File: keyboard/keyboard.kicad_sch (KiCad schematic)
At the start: 115 parts, among them J1 USB_C_Receptacle_USB2.0_14P, SW1 Keyswitch, SW10 Keyswitch, SW11 Keyswitch, SW12 Keyswitch, SW13 Keyswitch, SW14 Keyswitch, SW15 Keyswitch, SW16 Keyswitch, SW17 Keyswitch, SW18 Keyswitch, SW19 Keyswitch, SW2 Keyswitch, SW20 Keyswitch, SW21 Keyswitch, SW22 Keyswitch, SW23 Keyswitch, SW24 Keyswitch, SW25 Keyswitch, SW26 Keyswitch, SW27 Keyswitch, SW28 Keyswitch, SW29 Keyswitch, SW3 Keyswitch, SW30 Keyswitch, SW31 Keyswitch, SW32 Keyswitch, SW33 Keyswitch, SW34 Keyswitch, SW35 Keyswitch, SW36 Keyswitch, SW37 Keyswitch, SW38 Keyswitch, SW39 Keyswitch, SW4 Keyswitch, SW40 Keyswitch, SW41 Keyswitch, SW42 Keyswitch, SW43 Keyswitch, SW44 Keyswitch, SW45 Keyswitch, SW46 Keyswitch, SW47 Keyswitch, SW48 Keyswitch, SW5 Keyswitch, SW6 Keyswitch, SW7 Keyswitch, SW8 Keyswitch, SW9 Keyswitch, U1 STM32F072CBU7, U2 USBLC6-2P6, U3 AP2112K-3.3

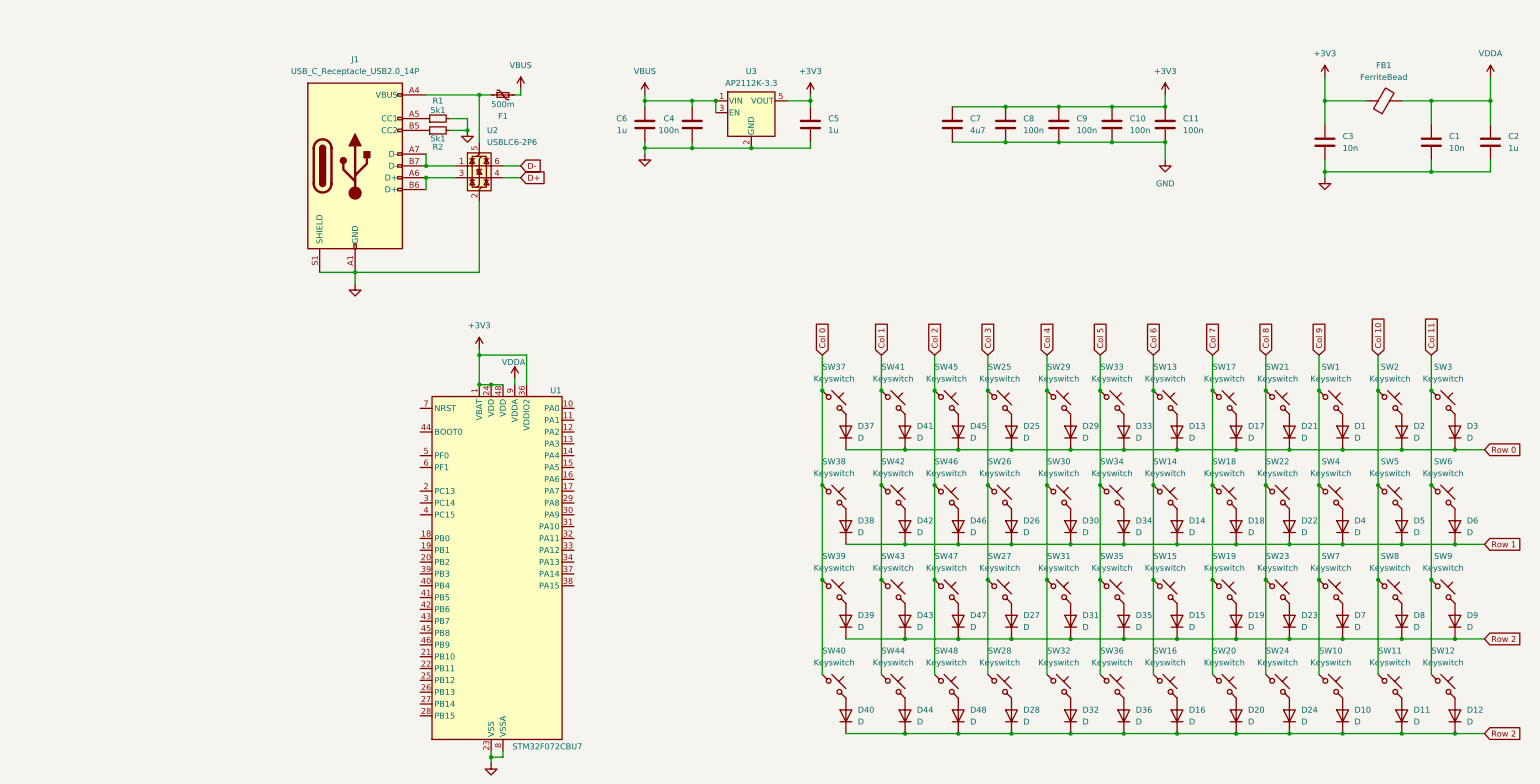
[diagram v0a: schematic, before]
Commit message: feat(keyboard): add boot, rst and usb
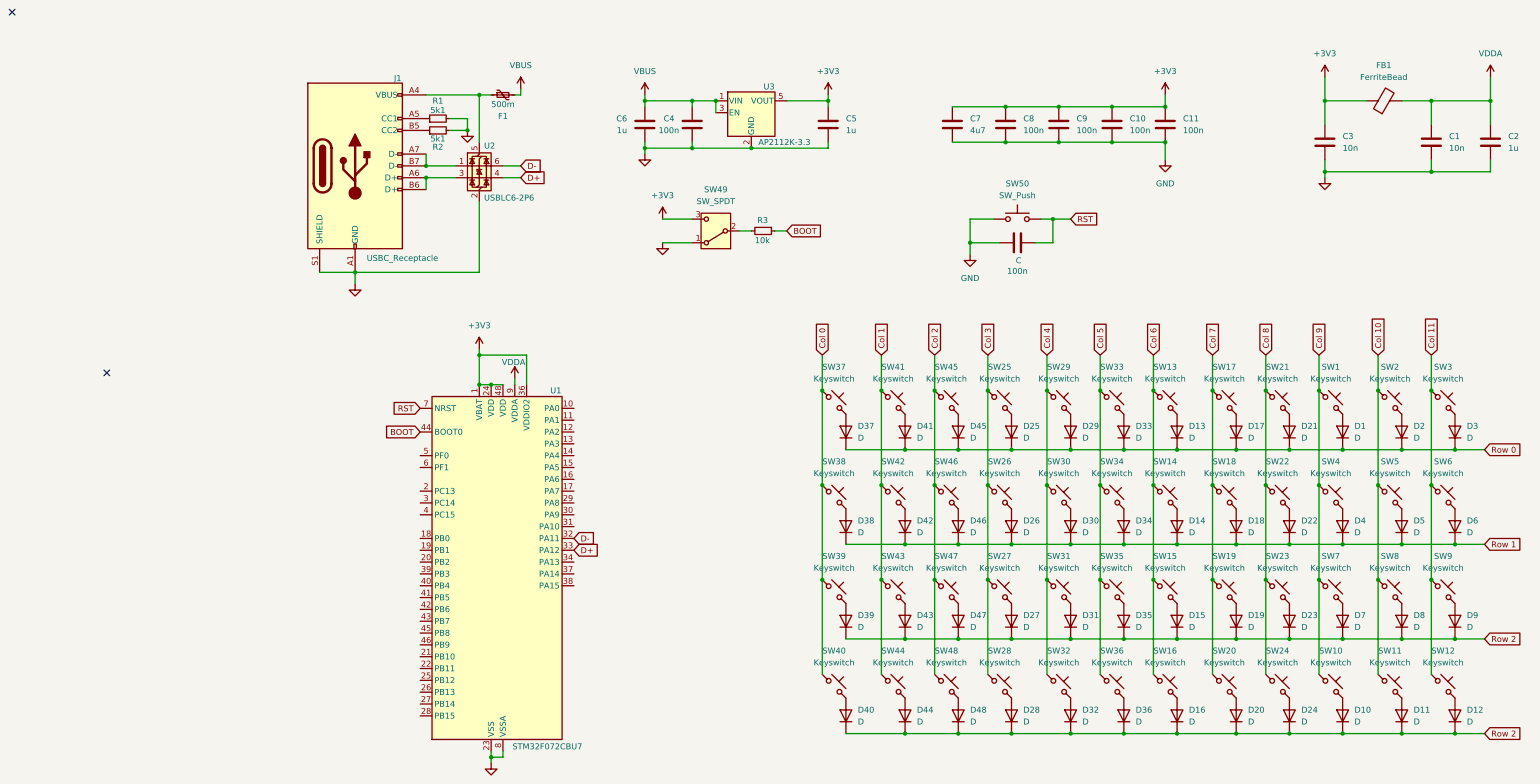
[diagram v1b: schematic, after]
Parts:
- added 100n: C, symbol Device:C
- added R3: 10k, symbol Device:R_Small
- added SW49: SW_SPDT, symbol Switch:SW_SPDT
- added SW50: SW_Push, symbol Switch:SW_Push
- J1: value USB_C_Receptacle_USB2.0_14P -> USBC_Receptacle
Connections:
- net +3V3: now also SW49.3 (C)
- net D+: now also U1.33 (PA12)
- net D-: now also U1.32 (PA11)
- net GND: now also 100n.2, SW49.1 (A), SW50.1
- net BOOT: now reaches U1.44 (BOOT0)
- net BOOT: now also R3.1
- net RST: now reaches U1.7 (NRST)
- net RST: now also 100n.1, SW50.2
- new net: R3.2, SW49.2 (B)
- no-connect marks 0 -> 2
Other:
- moved on the sheet: C5

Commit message: feat(keyboard): pcb route
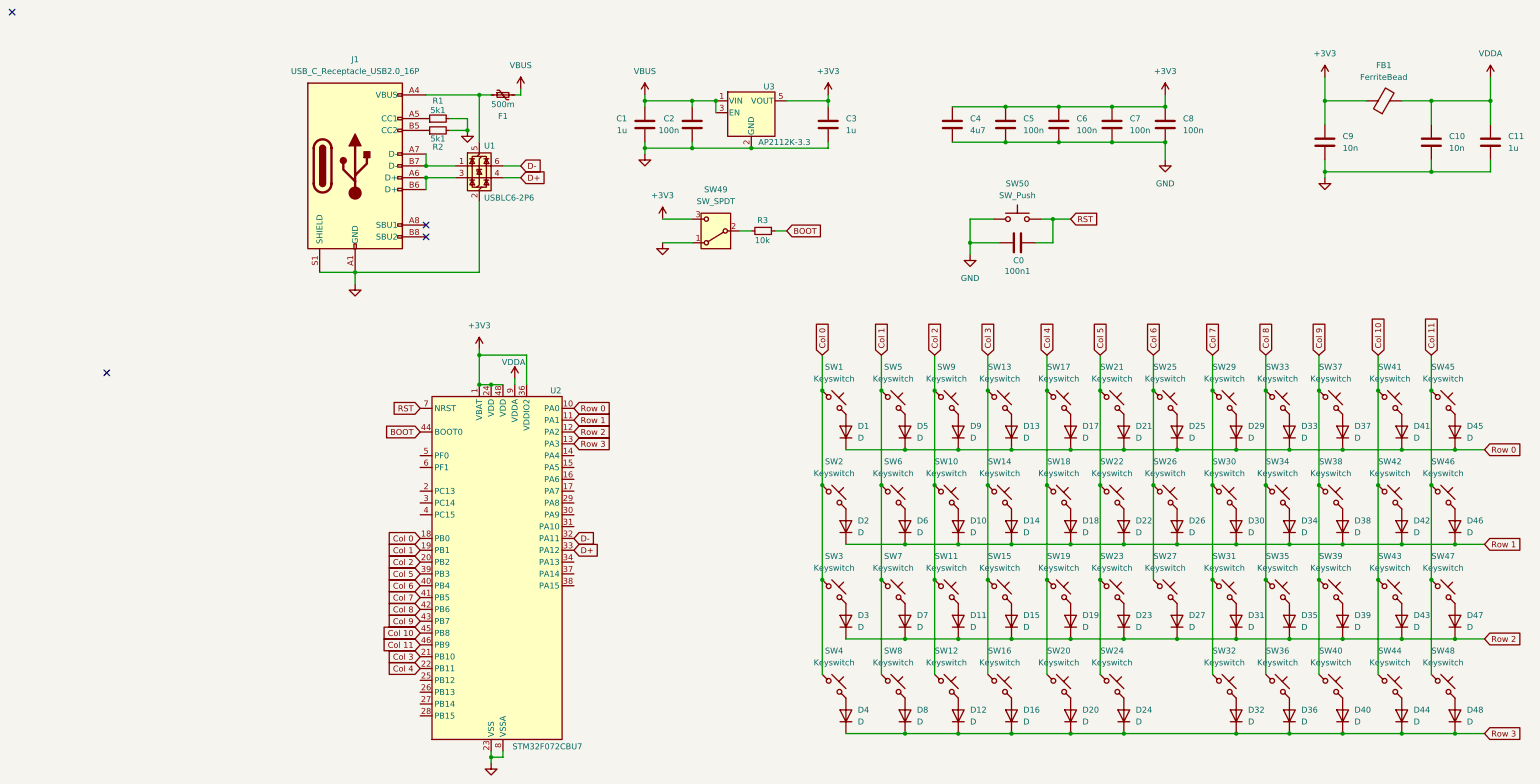
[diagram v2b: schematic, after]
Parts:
- removed D16: D, symbol Device:D
- removed J1: USBC_Receptacle, symbol Connector:USB_C_Receptacle_USB2.0_14P
- removed SW16: Keyswitch, symbol Switch:SW_Push_45deg
- added J1: USB_C_Receptacle_USB2.0_16P, Connector_USB:USB_C_Receptacle_GCT_USB4110, symbol Connector:USB_C_Receptacle_USB2.0_16P
- 100n1: renamed from 100n; value C -> C0; footprint (none) -> Capacitor_SMD:C_0201_0603Metric
- C1: renamed from C6; footprint (none) -> Capacitor_SMD:C_0201_0603Metric
- C10: renamed from C1; footprint (none) -> Capacitor_SMD:C_0201_0603Metric
- C11: renamed from C2; footprint (none) -> Capacitor_SMD:C_0201_0603Metric
- C2: renamed from C4; footprint (none) -> Capacitor_SMD:C_0201_0603Metric
- C3: renamed from C5; footprint (none) -> Capacitor_SMD:C_0201_0603Metric
- C4: renamed from C7; footprint (none) -> Capacitor_SMD:C_0201_0603Metric
- C5: renamed from C8; footprint (none) -> Capacitor_SMD:C_0201_0603Metric
- C6: renamed from C9; footprint (none) -> Capacitor_SMD:C_0201_0603Metric
- C7: renamed from C10; footprint (none) -> Capacitor_SMD:C_0201_0603Metric
- C8: renamed from C11; footprint (none) -> Capacitor_SMD:C_0201_0603Metric
- C9: renamed from C3; footprint (none) -> Capacitor_SMD:C_0201_0603Metric
- D1: renamed from D37; footprint (none) -> Diode_SMD:D_SOD-123
- D10: renamed from D46; footprint (none) -> Diode_SMD:D_SOD-123
- D11: renamed from D47; footprint (none) -> Diode_SMD:D_SOD-123
- D12: renamed from D48; footprint (none) -> Diode_SMD:D_SOD-123
- D13: renamed from D25; footprint (none) -> Diode_SMD:D_SOD-123
- D14: renamed from D26; footprint (none) -> Diode_SMD:D_SOD-123
- D15: renamed from D27; footprint (none) -> Diode_SMD:D_SOD-123
- D16: renamed from D28; footprint (none) -> Diode_SMD:D_SOD-123
- D17: renamed from D29; footprint (none) -> Diode_SMD:D_SOD-123
- D18: renamed from D30; footprint (none) -> Diode_SMD:D_SOD-123
- D19: renamed from D31; footprint (none) -> Diode_SMD:D_SOD-123
- D2: renamed from D38; footprint (none) -> Diode_SMD:D_SOD-123
- D20: renamed from D32; footprint (none) -> Diode_SMD:D_SOD-123
- D21: renamed from D33; footprint (none) -> Diode_SMD:D_SOD-123
- D22: renamed from D34; footprint (none) -> Diode_SMD:D_SOD-123
- D23: renamed from D35; footprint (none) -> Diode_SMD:D_SOD-123
- D24: renamed from D36; footprint (none) -> Diode_SMD:D_SOD-123
- D25: renamed from D13; footprint (none) -> Diode_SMD:D_SOD-123
- D26: renamed from D14; footprint (none) -> Diode_SMD:D_SOD-123
- D27: renamed from D15; footprint (none) -> Diode_SMD:D_SOD-123
- D29: renamed from D17; footprint (none) -> Diode_SMD:D_SOD-123
- D3: renamed from D39; footprint (none) -> Diode_SMD:D_SOD-123
- D30: renamed from D18; footprint (none) -> Diode_SMD:D_SOD-123
- D31: renamed from D19; footprint (none) -> Diode_SMD:D_SOD-123
- D32: renamed from D20; footprint (none) -> Diode_SMD:D_SOD-123
- D33: renamed from D21; footprint (none) -> Diode_SMD:D_SOD-123
- D34: renamed from D22; footprint (none) -> Diode_SMD:D_SOD-123
- D35: renamed from D23; footprint (none) -> Diode_SMD:D_SOD-123
- D36: renamed from D24; footprint (none) -> Diode_SMD:D_SOD-123
- D37: renamed from D1; footprint (none) -> Diode_SMD:D_SOD-123
- D38: renamed from D4; footprint (none) -> Diode_SMD:D_SOD-123
- D39: renamed from D7; footprint (none) -> Diode_SMD:D_SOD-123
- D4: renamed from D40; footprint (none) -> Diode_SMD:D_SOD-123
- D40: renamed from D10; footprint (none) -> Diode_SMD:D_SOD-123
- D41: renamed from D2; footprint (none) -> Diode_SMD:D_SOD-123
- D42: renamed from D5; footprint (none) -> Diode_SMD:D_SOD-123
- D43: renamed from D8; footprint (none) -> Diode_SMD:D_SOD-123
- D44: renamed from D11; footprint (none) -> Diode_SMD:D_SOD-123
- D45: renamed from D3; footprint (none) -> Diode_SMD:D_SOD-123
- D46: renamed from D6; footprint (none) -> Diode_SMD:D_SOD-123
- D47: renamed from D9; footprint (none) -> Diode_SMD:D_SOD-123
- D48: renamed from D12; footprint (none) -> Diode_SMD:D_SOD-123
- D5: renamed from D41; footprint (none) -> Diode_SMD:D_SOD-123
- D6: renamed from D42; footprint (none) -> Diode_SMD:D_SOD-123
- D7: renamed from D43; footprint (none) -> Diode_SMD:D_SOD-123
- D8: renamed from D44; footprint (none) -> Diode_SMD:D_SOD-123
- D9: renamed from D45; footprint (none) -> Diode_SMD:D_SOD-123
- F1: footprint (none) -> Fuse:Fuse_0603_1608Metric
- FB1: footprint (none) -> Inductor_SMD:L_0201_0603Metric
- R1, R2, R3: footprint (none) -> Resistor_SMD:R_0201_0603Metric
- SW1: renamed from SW37; footprint (none) -> PCM_Switch_Keyboard_Hotswap_Kailh:SW_Hotswap_Kailh_MX_1.00u
- SW10: renamed from SW46; footprint (none) -> PCM_Switch_Keyboard_Hotswap_Kailh:SW_Hotswap_Kailh_MX_1.00u
- SW11: renamed from SW47; footprint (none) -> PCM_Switch_Keyboard_Hotswap_Kailh:SW_Hotswap_Kailh_MX_1.00u
- SW12: renamed from SW48; footprint (none) -> PCM_Switch_Keyboard_Hotswap_Kailh:SW_Hotswap_Kailh_MX_1.00u
- SW13: renamed from SW25; footprint (none) -> PCM_Switch_Keyboard_Hotswap_Kailh:SW_Hotswap_Kailh_MX_1.00u
- SW14: renamed from SW26; footprint (none) -> PCM_Switch_Keyboard_Hotswap_Kailh:SW_Hotswap_Kailh_MX_1.00u
- SW15: renamed from SW27; footprint (none) -> PCM_Switch_Keyboard_Hotswap_Kailh:SW_Hotswap_Kailh_MX_1.00u
- SW16: renamed from SW28; footprint (none) -> PCM_Switch_Keyboard_Hotswap_Kailh:SW_Hotswap_Kailh_MX_1.00u
- SW17: renamed from SW29; footprint (none) -> PCM_Switch_Keyboard_Hotswap_Kailh:SW_Hotswap_Kailh_MX_1.00u
- SW18: renamed from SW30; footprint (none) -> PCM_Switch_Keyboard_Hotswap_Kailh:SW_Hotswap_Kailh_MX_1.00u
- SW19: renamed from SW31; footprint (none) -> PCM_Switch_Keyboard_Hotswap_Kailh:SW_Hotswap_Kailh_MX_1.00u
- SW2: renamed from SW38; footprint (none) -> PCM_Switch_Keyboard_Hotswap_Kailh:SW_Hotswap_Kailh_MX_1.00u
- SW20: renamed from SW32; footprint (none) -> PCM_Switch_Keyboard_Hotswap_Kailh:SW_Hotswap_Kailh_MX_1.00u
- SW21: renamed from SW33; footprint (none) -> PCM_Switch_Keyboard_Hotswap_Kailh:SW_Hotswap_Kailh_MX_1.00u
- SW22: renamed from SW34; footprint (none) -> PCM_Switch_Keyboard_Hotswap_Kailh:SW_Hotswap_Kailh_MX_1.00u
- SW23: renamed from SW35; footprint (none) -> PCM_Switch_Keyboard_Hotswap_Kailh:SW_Hotswap_Kailh_MX_1.00u
- SW24: renamed from SW36; footprint (none) -> PCM_Switch_Keyboard_Hotswap_Kailh:SW_Hotswap_Kailh_MX_2.00u
- SW25: renamed from SW13; footprint (none) -> PCM_Switch_Keyboard_Hotswap_Kailh:SW_Hotswap_Kailh_MX_1.00u
- SW26: renamed from SW14; footprint (none) -> PCM_Switch_Keyboard_Hotswap_Kailh:SW_Hotswap_Kailh_MX_1.00u
- SW27: renamed from SW15; footprint (none) -> PCM_Switch_Keyboard_Hotswap_Kailh:SW_Hotswap_Kailh_MX_1.00u
- SW29: renamed from SW17; footprint (none) -> PCM_Switch_Keyboard_Hotswap_Kailh:SW_Hotswap_Kailh_MX_1.00u
- SW3: renamed from SW39; footprint (none) -> PCM_Switch_Keyboard_Hotswap_Kailh:SW_Hotswap_Kailh_MX_1.00u
- SW30: renamed from SW18; footprint (none) -> PCM_Switch_Keyboard_Hotswap_Kailh:SW_Hotswap_Kailh_MX_1.00u
- SW31: renamed from SW19; footprint (none) -> PCM_Switch_Keyboard_Hotswap_Kailh:SW_Hotswap_Kailh_MX_1.00u
- SW32: renamed from SW20; footprint (none) -> PCM_Switch_Keyboard_Hotswap_Kailh:SW_Hotswap_Kailh_MX_1.00u
- SW33: renamed from SW21; footprint (none) -> PCM_Switch_Keyboard_Hotswap_Kailh:SW_Hotswap_Kailh_MX_1.00u
- SW34: renamed from SW22; footprint (none) -> PCM_Switch_Keyboard_Hotswap_Kailh:SW_Hotswap_Kailh_MX_1.00u
- SW35: renamed from SW23; footprint (none) -> PCM_Switch_Keyboard_Hotswap_Kailh:SW_Hotswap_Kailh_MX_1.00u
- SW36: renamed from SW24; footprint (none) -> PCM_Switch_Keyboard_Hotswap_Kailh:SW_Hotswap_Kailh_MX_1.00u
- SW37: renamed from SW1; footprint (none) -> PCM_Switch_Keyboard_Hotswap_Kailh:SW_Hotswap_Kailh_MX_1.00u
- SW38: renamed from SW4; footprint (none) -> PCM_Switch_Keyboard_Hotswap_Kailh:SW_Hotswap_Kailh_MX_1.00u
- SW39: renamed from SW7; footprint (none) -> PCM_Switch_Keyboard_Hotswap_Kailh:SW_Hotswap_Kailh_MX_1.00u
- SW4: renamed from SW40; footprint (none) -> PCM_Switch_Keyboard_Hotswap_Kailh:SW_Hotswap_Kailh_MX_1.00u
- SW40: renamed from SW10; footprint (none) -> PCM_Switch_Keyboard_Hotswap_Kailh:SW_Hotswap_Kailh_MX_1.00u
- SW41: renamed from SW2; footprint (none) -> PCM_Switch_Keyboard_Hotswap_Kailh:SW_Hotswap_Kailh_MX_1.00u
- SW42: renamed from SW5; footprint (none) -> PCM_Switch_Keyboard_Hotswap_Kailh:SW_Hotswap_Kailh_MX_1.00u
- SW43: renamed from SW8; footprint (none) -> PCM_Switch_Keyboard_Hotswap_Kailh:SW_Hotswap_Kailh_MX_1.00u
- SW44: renamed from SW11; footprint (none) -> PCM_Switch_Keyboard_Hotswap_Kailh:SW_Hotswap_Kailh_MX_1.00u
- SW45: renamed from SW3; footprint (none) -> PCM_Switch_Keyboard_Hotswap_Kailh:SW_Hotswap_Kailh_MX_1.00u
- SW46: renamed from SW6; footprint (none) -> PCM_Switch_Keyboard_Hotswap_Kailh:SW_Hotswap_Kailh_MX_1.00u
- SW47: renamed from SW9; footprint (none) -> PCM_Switch_Keyboard_Hotswap_Kailh:SW_Hotswap_Kailh_MX_1.00u
- SW48: renamed from SW12; footprint (none) -> PCM_Switch_Keyboard_Hotswap_Kailh:SW_Hotswap_Kailh_MX_1.00u
- SW49: footprint (none) -> Button_Switch_SMD:SW_SPDT_PCM12
- SW5: renamed from SW41; footprint (none) -> PCM_Switch_Keyboard_Hotswap_Kailh:SW_Hotswap_Kailh_MX_1.00u
- SW50: footprint (none) -> Button_Switch_SMD:SW_SPST_SKQG_WithStem
- SW6: renamed from SW42; footprint (none) -> PCM_Switch_Keyboard_Hotswap_Kailh:SW_Hotswap_Kailh_MX_1.00u
- SW7: renamed from SW43; footprint (none) -> PCM_Switch_Keyboard_Hotswap_Kailh:SW_Hotswap_Kailh_MX_1.00u
- SW8: renamed from SW44; footprint (none) -> PCM_Switch_Keyboard_Hotswap_Kailh:SW_Hotswap_Kailh_MX_1.00u
- SW9: renamed from SW45; footprint (none) -> PCM_Switch_Keyboard_Hotswap_Kailh:SW_Hotswap_Kailh_MX_1.00u
- renumbered U2 to U1, U1 to U2
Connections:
- net Col 0: now also U2.18 (PB0)
- net Col 1: now also U2.19 (PB1)
- net Col 10: now also U2.45 (PB8)
- net Col 11: now also U2.46 (PB9)
- net Col 2: now also U2.20 (PB2)
- net Col 3: now also U2.21 (PB10)
- net Col 4: now also U2.22 (PB11)
- net Col 5: now also U2.39 (PB3)
- net Col 6: now also U2.40 (PB4)
- net Col 7: now also U2.41 (PB5)
- net Col 8: now also U2.42 (PB6)
- net Col 9: now also U2.43 (PB7)
- net GND: now also J1.A1 (GND), J1.A12 (GND), J1.B1 (GND), J1.B12 (GND), J1.S1 (SHIELD)
- net Row 0: now also U2.10 (PA0)
- net Row 1: now also U2.11 (PA1)
- net Row 2: now also U2.12 (PA2); no longer D12.1 (K), D16.1 (K), D20.1 (K), D24.1 (K), D32.1 (K), D36.1 (K), D4.1 (K), D40.1 (K), D44.1 (K), D48.1 (K), D8.1 (K)
- net at U1.1 (I/O1): now also J1.A7 (D-), J1.B7 (D-)
- net at U1.3 (I/O2): now also J1.A6 (D+), J1.B6 (D+)
- net at F1.1, U1.5 (VBUS): now also J1.A4 (VBUS), J1.A9 (VBUS), J1.B4 (VBUS), J1.B9 (VBUS)
- net Row 3: now reaches U2.13 (PA3)
- net Row 3: now also D12.1 (K), D16.1 (K), D20.1 (K), D24.1 (K), D32.1 (K), D36.1 (K), D4.1 (K), D40.1 (K), D44.1 (K), D48.1 (K), D8.1 (K)
- net at R2.1: now also J1.B5 (CC2)
- net at R1.1: now also J1.A5 (CC1)
- no-connect marks 2 -> 4

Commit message: feat(keyboard): finish route, edges and silk
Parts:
- SW1, SW10, SW11, SW12, SW13, SW14, SW15, SW16, SW17, SW18, SW19, SW2, SW20, SW21, SW22, SW23, SW25, SW26, SW27, SW29, SW3, SW30, SW31, SW32, SW33, SW34, SW35, SW36, SW37, SW38, SW39, SW4, SW40, SW41, SW42, SW43, SW44, SW45, SW46, SW47, SW48, SW5, SW6, SW7, SW8, SW9: footprint PCM_Switch_Keyboard_Hotswap_Kailh:SW_Hotswap_Kailh_MX_1.00u -> PCM_Switch_Keyboard_Hotswap_Kailh:SW_Hotswap_Kailh_MX
- SW24: footprint PCM_Switch_Keyboard_Hotswap_Kailh:SW_Hotswap_Kailh_MX_2.00u -> PCM_Switch_Keyboard_Hotswap_Kailh:SW_Hotswap_Kailh_MX

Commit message: feat(keyboard): fix bom and cpl
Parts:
- C0: renamed from 100n1; value C0 -> 100n; footprint Capacitor_SMD:C_0201_0603Metric -> Capacitor_SMD:C_0603_1608Metric; JLC (none) -> 0603; LCSC (none) -> C2909627
- C1, C11, C3: footprint Capacitor_SMD:C_0201_0603Metric -> Capacitor_SMD:C_0603_1608Metric; JLC (none) -> 0603; LCSC (none) -> C2691405
- C10, C9: footprint Capacitor_SMD:C_0201_0603Metric -> Capacitor_SMD:C_0603_1608Metric; JLC (none) -> 0603; LCSC (none) -> C185599
- C2, C5, C6, C7, C8: footprint Capacitor_SMD:C_0201_0603Metric -> Capacitor_SMD:C_0603_1608Metric; JLC (none) -> 0603; LCSC (none) -> C2909627
- C4: footprint Capacitor_SMD:C_0201_0603Metric -> Capacitor_SMD:C_0603_1608Metric; JLC (none) -> 0603; LCSC (none) -> C2918512
- D1, D10, D11, D12, D13, D14, D15, D16, D17, D18, D19, D2, D20, D21, D22, D23, D24, D25, D26, D27, D29, D3, D30, D31, D32, D33, D34, D35, D36, D37, D38, D39, D4, D40, D41, D42, D43, D44, D45, D46, D47, D48, D5, D6, D7, D8, D9: JLC (none) -> SOD-123; LCSC (none) -> C402213
- F1: JLC (none) -> 0603; LCSC (none) -> C3760867
- FB1: footprint Inductor_SMD:L_0201_0603Metric -> Inductor_SMD:L_0603_1608Metric; JLC (none) -> 0603; LCSC (none) -> C491555
- J1: footprint Connector_USB:USB_C_Receptacle_GCT_USB4110 -> Connector_USB:USB_C_Receptacle_XKB_U262-16XN-4BVC11; JLC (none) -> SMD; LCSC (none) -> C319148
- R1, R2: footprint Resistor_SMD:R_0201_0603Metric -> Resistor_SMD:R_0603_1608Metric; JLC (none) -> 0603; LCSC (none) -> C543856
- R3: footprint Resistor_SMD:R_0201_0603Metric -> Resistor_SMD:R_0603_1608Metric; JLC (none) -> 0603; LCSC (none) -> C328335
- SW1, SW10, SW11, SW12, SW13, SW14, SW15, SW16, SW17, SW18, SW19, SW2, SW20, SW21, SW22, SW23, SW24, SW25, SW26, SW27, SW29, SW3, SW30, SW31, SW32, SW33, SW34, SW35, SW36, SW37, SW38, SW39, SW4, SW40, SW41, SW42, SW43, SW44, SW45, SW46, SW47, SW48, SW5, SW6, SW7, SW8, SW9: JLC (none) -> SMD; LCSC (none) -> C2803348
- SW49: JLC (none) -> SMD; LCSC (none) -> C221841
- SW50: JLC (none) -> SMD; LCSC (none) -> C202424
- U1: JLC (none) -> SOT-666-6; LCSC (none) -> C2827693
- U2: value STM32F072CBU7 -> STM32F072CBU6; JLC (none) -> UFQFPN-48(7x7); LCSC (none) -> C1342708
- U3: JLC (none) -> SOT-23-5; LCSC (none) -> C3021085
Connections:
- net Col 0: now also U2.16 (PA6); no longer U2.18 (PB0)
- net Col 1: now also U2.17 (PA7); no longer U2.19 (PB1)
- net Col 2: now also U2.18 (PB0); no longer U2.20 (PB2)
- net Col 3: now also U2.19 (PB1); no longer U2.21 (PB10)
- net Col 4: now also U2.20 (PB2); no longer U2.22 (PB11)
- net Col 5: now also U2.21 (PB10); no longer U2.39 (PB3)
- net Col 6: now also U2.22 (PB11); no longer U2.40 (PB4)
- net Row 0: now also U2.15 (PA5); no longer U2.10 (PA0)
- net Row 1: now also U2.14 (PA4); no longer U2.11 (PA1)
- net Row 2: now also U2.13 (PA3); no longer U2.12 (PA2)
- net Row 3: now also U2.12 (PA2); no longer U2.13 (PA3)
